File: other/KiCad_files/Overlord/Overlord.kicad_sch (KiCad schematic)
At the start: 108 parts, among them J1 RJ45x2, J2 Screw_Terminal_01x09, J3 Conn_01x12_Female, J4 Screw_Terminal_01x09, J5 Screw_Terminal_01x09, J6 Screw_Terminal_01x09, J7 USB_B, J8 USB_cable, Q1 2N7002E, Q2 2N7002E, Q3 2N7002E, Q4 2N7002E, U1 74HC4052D,653, U2 74HC4052D,653, U3 74HC4052D,653, U4 74HC4052D,653, U5 LM2575D2T-5G, U6 SN65HVD230, U7 MAX485ESA+T, U8 AP63203WU-7, U9 MAX485ESA+T

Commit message: temp changes
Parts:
- L2: footprint Inductor_SMD:L_Bourns-SRU8028_8.0x8.0mm -> (none)
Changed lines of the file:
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@@
       (effects (font (size 1.27 1.27)))
     )
-    (property "Footprint" "Inductor_SMD:L_Bourns-SRU8028_8.0x8.0mm" (at 60.96 247.65 0)
+    (property "Footprint" "" (at 60.96 247.65 0)
       (effects (font (size 1.27 1.27)) hide)
     )

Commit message: pre ESP32-S3 migration
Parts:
- U7, U9: value MAX485ESA+T -> MAX485ESA+T

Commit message: sent to production
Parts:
- removed 120R_enable1: Conn_01x02_Male, Connector_PinHeader_2.54mm:PinHeader_1x02_P2.54mm_Vertical, symbol Connector:Conn_01x02_Pin
- removed C1: 100uF, Capacitor_SMD:C_Elec_6.3x7.7, symbol Device:C_Polarized
- removed C17, C2, C3: 10uF, Capacitor_THT:CP_Radial_D4.0mm_P1.50mm, symbol Device:C_Polarized
- removed C18, C19, C20, C21, C22, C23, C24, C25, C26, C28, C29, C30, C31, C32, C33, C34, C35, C36, C37, C38, C39, C40, C41, C42, C43: 100nF, Capacitor_THT:C_Disc_D6.0mm_W2.5mm_P5.00mm, symbol Device:C
- removed C27, C44, C45: 220uF, Capacitor_THT:CP_Radial_D8.0mm_P3.50mm, symbol Device:C
- removed C5, C6: 22uF, Capacitor_THT:CP_Radial_D4.0mm_P1.50mm, symbol Device:C_Polarized
- removed D1: 1N5819, Diode_SMD:D_SOD-123, symbol Device:D_Schottky
- removed D2: SBR1A40S1, Diode_SMD:D_SOD-123, symbol Device:D
- removed ESP1: ESP-DevKitC-V4, Overlord:ESP32-DevKitC-V4, symbol MCU_Espressif_ESP32:ESP-DevKitC-V4
- removed J1: RJ45x2, Connector_RJ:RJ45_Amphenol_RJHSE538X-02, symbol Overlord-cache:74HC251D,653_RJ45x2
- removed J2, J5, J6: Screw_Terminal_01x09, TerminalBlockCustom:TerminalBlock_9_5.08mm_inverted, symbol Connector:Screw_Terminal_01x09
- removed J3: Conn_01x12_Female, Connector_Molex:Molex_CLIK-Mate_502386-1270_1x12-1MP_P1.25mm_Horizontal, symbol Connector_Generic_MountingPin:Conn_01x12_MountingPin
- removed J4: Screw_Terminal_01x09, TerminalBlockCustom:TerminalBlock_9_5.08mm, symbol Connector:Screw_Terminal_01x09
- removed J7: USB_B, Connector_USB:USB_B_OST_USB-B1HSxx_Horizontal, symbol Connector:USB_B
- removed J8: USB_cable, Connector_PinHeader_2.54mm:PinHeader_1x04_P2.54mm_Vertical, symbol Overlord-cache:Connector_Conn_01x04_Male
- removed L1: 7447709331, Inductor_SMD:L_12x12mm_H8mm, symbol Device:L
- removed L2: 4.7uH, symbol Device:L
- removed Q1, Q2, Q3, Q4: 2N7002E, Package_TO_SOT_SMD:SOT-23, symbol Transistor_FET:2N7002E
- removed R15: 10K, Resistor_SMD:R_0805_2012Metric_Pad1.20x1.40mm_HandSolder, symbol Device:R
- removed R16: 220, Resistor_SMD:R_0805_2012Metric_Pad1.20x1.40mm_HandSolder, symbol Device:R
- removed R31, R33: 5K, Resistor_SMD:R_0805_2012Metric_Pad1.20x1.40mm_HandSolder, symbol Device:R
- removed R6: 20K, Resistor_SMD:R_1812_4532Metric_Pad1.30x3.40mm_HandSolder, symbol Device:R
- removed R7: 120, Resistor_SMD:R_1812_4532Metric_Pad1.30x3.40mm_HandSolder, symbol Device:R
- removed RN1, RN2, RN3, RN4, RN5, RN6, RN7, RN8: Res_network 4.7kOhm, Resistor_SMD:R_Array_Convex_4x0612, symbol Device:R_Pack04
- removed U1, U2, U3, U4: 74HC4052D,653, Package_SO:SO-16_3.9x9.9mm_P1.27mm, symbol Overlord-cache:74HC251D,653_74HC4052D,653
- removed U5: LM2575D2T-5G, Package_TO_SOT_SMD:TO-263-5_TabPin3, symbol Regulator_Switching:LM2575-5.0BU
- removed U6: SN65HVD230, Package_SO:SOIC-8_3.9x4.9mm_P1.27mm, symbol Interface_CAN_LIN:SN65HVD230
- removed U8: AP63203WU-7, Package_TO_SOT_SMD:TSOT-23-6, symbol Regulator_Switching:AP63203WU
- added 12VLED1, 3V3LED1, 5VLED1: LED, LED_SMD:LED_0805_2012Metric_Pad1.15x1.40mm_HandSolder, symbol Device:LED
- added BOOT1, RESET1: PTS810SJK250SMTR LFS, OverlordCommon:PTS810SJK250SMTRLFS, symbol Switch:SW_MEC_5E
- added C1, C17, C3: 0.1uF, Capacitor_SMD:C_0805_2012Metric_Pad1.18x1.45mm_HandSolder, symbol Device:C
- added C11, C2: 10uF, Capacitor_SMD:C_0805_2012Metric_Pad1.18x1.45mm_HandSolder, symbol Device:C
- added C5, C6: 1uF, Capacitor_SMD:C_0805_2012Metric_Pad1.18x1.45mm_HandSolder, symbol Device:C
- added D1, D2, D3, D4, D5, D6: 1N4148, Diode_SMD:D_0805_2012Metric_Pad1.15x1.40mm_HandSolder, symbol Diode:1N4148
- added D7: TPD2E001DZDR, OverlordCommon:TPD2E001DZDR, symbol TPD2E001DZDR:TPD2E001DZDR
- added DB9_IN1: 5788792-2, OverlordCommon:5788792, symbol 5788792-2:5788792-2
- added DB9_OUT1: 5747844-4, OverlordCommon:57478444, symbol 5747844-4:5747844-4
- added Dbg1, Dbg10, Dbg11, Dbg12, Dbg13, Dbg14, Dbg15, Dbg16, Dbg17, Dbg18, Dbg19, Dbg2, Dbg20, Dbg21, Dbg22, Dbg23, Dbg24, Dbg25, Dbg26, Dbg27, Dbg28, Dbg29, Dbg3, Dbg30, Dbg31, Dbg32, Dbg33, Dbg34, Dbg4, Dbg5, Dbg6, Dbg7, Dbg8, Dbg9: Connector_Conn_01x01_Male, Connector_PinHeader_2.54mm:PinHeader_1x01_P2.54mm_Vertical, symbol Overlord-cache:Connector_Conn_01x01_Male
- added J1, J2, J3: 39502-1011, OverlordCommon:SHDRRA11W80P0X350_1X11_3990X690X920P, symbol 39502-1011:39502-1011
- added J4: Conn_01x12_Pin, Connector_Molex:Molex_Picoflex_90325-0012_2x06_P1.27mm_Vertical, symbol Connector:Conn_01x12_Pin
- added J5: Conn_01x10_Pin, Connector_PinHeader_2.54mm:PinHeader_1x10_P2.54mm_Vertical, symbol Connector:Conn_01x10_Pin
- added J6, J7: Conn_01x11_Pin, Connector_PinHeader_2.54mm:PinHeader_1x11_P2.54mm_Vertical, symbol Connector:Conn_01x11_Pin
- added JP1, JP10, JP11, JP12, JP13, JP14, JP15, JP16, JP17, JP18, JP19, JP2, JP20, JP21, JP22, JP23, JP24, JP25, JP26, JP27, JP28, JP29, JP3, JP30, JP31, JP32, JP33, JP34, JP35, JP36, JP37, JP38, JP39, JP4, JP40, JP41, JP42, JP43, JP44, JP45, JP46, JP47, JP48, JP49, JP5, JP50, JP51, JP52, JP53, JP6, JP7, JP8, JP9: SolderJumper_2_Open, Jumper:SolderJumper-2_P1.3mm_Open_RoundedPad1.0x1.5mm, symbol Jumper:SolderJumper_2_Open
- added J_CAN120R1: Conn_01x02_Male, Connector_PinHeader_2.54mm:PinHeader_1x02_P2.54mm_Vertical, symbol Connector:Conn_01x02_Pin
- added J_JTAG1: FTSH-105-01-S-DV-K, OverlordCommon:FTSH-105-XX-YYY-DV-K, symbol FTSH-105-01-S-DV-K:FTSH-105-01-S-DV-K
- added J_JTAG3V3_1, J_PROG3V3_1: Conn_01x02_Pin, Connector_PinHeader_2.54mm:PinHeader_1x02_P2.54mm_Vertical, symbol Connector:Conn_01x02_Pin
- added J_PROG1: FTSH-103-01-S-DV-TR, OverlordCommon:FTSH-103-XX-YYY-DV-TR, symbol FTSH-103-01-S-DV-TR:FTSH-103-01-S-DV-TR
- added J_USB1: USB_B, OverlordCommon:USB, symbol Connector:USB_B
- added R11: 240, Resistor_SMD:R_0805_2012Metric, symbol Device:R
- added R12: 10k, Resistor_SMD:R_0805_2012Metric_Pad1.20x1.40mm_HandSolder, symbol Device:R
- added R13: 499, Resistor_SMD:R_0805_2012Metric_Pad1.20x1.40mm_HandSolder, symbol Device:R
- added R14: 147, Resistor_SMD:R_0805_2012Metric_Pad1.20x1.40mm_HandSolder, symbol Device:R
- added R19, R20: 220, Resistor_SMD:R_0805_2012Metric_Pad1.20x1.40mm_HandSolder, symbol Device:R
- added SN65HVD230_1: SN65HVD230, Package_SO:SOIC-8_3.9x4.9mm_P1.27mm, symbol Interface_CAN_LIN:SN65HVD230
- added SYM1, SYM2, SYM3: Terminal plug, OverlordCommon:39500-0011, symbol Graphic:Logo_Open_Hardware_Small
- added SYM4, SYM5: N6_logo_medium, OverlordCommon:Symbol_N6Industries_medium, symbol Graphic:Logo_Open_Hardware_Small
- added SYM6: WEEE, Symbol:WEEE-Logo_5.6x8mm_SilkScreen, symbol Graphic:Logo_Open_Hardware_Small
- added SYM7: CE, Symbol:CE-Logo_8.5x6mm_SilkScreen, symbol Graphic:Logo_Open_Hardware_Small
- added U_ESP32-S3-WROOM-1U-N16_1: ESP32S3-Wroom, PCM_Espressif:ESP32-S3-WROOM-1U, symbol ESP32S3-wroom:ESP32S3-Wroom
- added U_LM317_1, U_LM317_2: LM317_SOT-223, Package_TO_SOT_SMD:SOT-223-3_TabPin2, symbol Regulator_Linear:LM317_SOT-223
- added U_TRS3232EIPWR1: TRS3232EIPWR, OverlordCommon:SOP65P640X120-16N, symbol TRS3232EIPWR:TRS3232EIPWR
- C10: value 100nF -> 10uF; footprint Capacitor_THT:C_Disc_D6.0mm_W2.5mm_P5.00mm -> Capacitor_SMD:C_0805_2012Metric_Pad1.18x1.45mm_HandSolder
- C12, C14, C15, C16, C8, C9: value 100nF -> 0.1uF; footprint Capacitor_THT:C_Disc_D6.0mm_W2.5mm_P5.00mm -> Capacitor_SMD:C_0805_2012Metric_Pad1.18x1.45mm_HandSolder
- C13: value 220uF -> 0.1uF; footprint Capacitor_THT:CP_Radial_D8.0mm_P3.50mm -> Capacitor_SMD:C_0805_2012Metric_Pad1.18x1.45mm_HandSolder
- C4: value 100nF -> 1uF; footprint Capacitor_SMD:C_1812_4532Metric_Pad1.57x3.40mm_HandSolder -> Capacitor_SMD:C_0805_2012Metric_Pad1.18x1.45mm_HandSolder
- C7: value 100nF -> 1uF; footprint Capacitor_THT:C_Disc_D6.0mm_W2.5mm_P5.00mm -> Capacitor_SMD:C_0805_2012Metric_Pad1.18x1.45mm_HandSolder
- H1, H2: now left out of the parts list
- R1: value 5K -> 240; footprint Resistor_SMD:R_0805_2012Metric_Pad1.20x1.40mm_HandSolder -> Resistor_SMD:R_0805_2012Metric
- R10: renamed from R26; footprint Resistor_SMD:R_1812_4532Metric_Pad1.30x3.40mm_HandSolder -> Resistor_SMD:R_0805_2012Metric_Pad1.20x1.40mm_HandSolder
- R15: renamed from R25; footprint Resistor_SMD:R_1812_4532Metric_Pad1.30x3.40mm_HandSolder -> Resistor_SMD:R_0805_2012Metric_Pad1.20x1.40mm_HandSolder
- R16: renamed from R30; footprint Resistor_SMD:R_1812_4532Metric_Pad1.30x3.40mm_HandSolder -> Resistor_SMD:R_0805_2012Metric_Pad1.20x1.40mm_HandSolder
- R17: value 220 -> 680; footprint Resistor_SMD:R_0805_2012Metric_Pad1.20x1.40mm_HandSolder -> Resistor_SMD:R_0805_2012Metric
- R2: value 5K -> 120
- R21: renamed from R13; footprint Resistor_SMD:R_1812_4532Metric_Pad1.30x3.40mm_HandSolder -> Resistor_SMD:R_0805_2012Metric_Pad1.20x1.40mm_HandSolder
- R22: renamed from R8; footprint Resistor_SMD:R_1812_4532Metric_Pad1.30x3.40mm_HandSolder -> Resistor_SMD:R_0805_2012Metric_Pad1.20x1.40mm_HandSolder
- R23: renamed from R11; footprint Resistor_SMD:R_1812_4532Metric_Pad1.30x3.40mm_HandSolder -> Resistor_SMD:R_0805_2012Metric_Pad1.20x1.40mm_HandSolder
- R24: renamed from R12; footprint Resistor_SMD:R_1812_4532Metric_Pad1.30x3.40mm_HandSolder -> Resistor_SMD:R_0805_2012Metric_Pad1.20x1.40mm_HandSolder
- R25: renamed from R10; footprint Resistor_SMD:R_1812_4532Metric_Pad1.30x3.40mm_HandSolder -> Resistor_SMD:R_0805_2012Metric_Pad1.20x1.40mm_HandSolder
- R26: renamed from R9; footprint Resistor_SMD:R_1812_4532Metric_Pad1.30x3.40mm_HandSolder -> Resistor_SMD:R_0805_2012Metric_Pad1.20x1.40mm_HandSolder
- R27: renamed from R14; footprint Resistor_SMD:R_1812_4532Metric_Pad1.30x3.40mm_HandSolder -> Resistor_SMD:R_0805_2012Metric_Pad1.20x1.40mm_HandSolder
- R3: value 10K -> 0R
- R4: value 10K -> 60
- R5: value 10K -> 390; footprint Resistor_SMD:R_0805_2012Metric_Pad1.20x1.40mm_HandSolder -> Resistor_SMD:R_0805_2012Metric
- R6: renamed from R29; footprint Resistor_SMD:R_1812_4532Metric_Pad1.30x3.40mm_HandSolder -> Resistor_SMD:R_0805_2012Metric_Pad1.20x1.40mm_HandSolder
- R7: renamed from R24; footprint Resistor_SMD:R_1812_4532Metric_Pad1.30x3.40mm_HandSolder -> Resistor_SMD:R_0805_2012Metric_Pad1.20x1.40mm_HandSolder
- R8: renamed from R27; footprint Resistor_SMD:R_1812_4532Metric_Pad1.30x3.40mm_HandSolder -> Resistor_SMD:R_0805_2012Metric_Pad1.20x1.40mm_HandSolder
- R9: renamed from R28; footprint Resistor_SMD:R_1812_4532Metric_Pad1.30x3.40mm_HandSolder -> Resistor_SMD:R_0805_2012Metric_Pad1.20x1.40mm_HandSolder
- renumbered U9 to MAX485ESA+T_1, U7 to MAX485ESA+T_2
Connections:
- net +12V: now also 12VLED1.2 (A), D2.2 (A), D6.2 (A), DB9_IN1.9, DB9_OUT1.9, Dbg33.1 (Pin_1); no longer R1.2, R2.2
- net +3.3V: now also C13.1, R1.1, 3V3LED1.2 (A), C1.1, C2.2, C3.1, C5.1, D1.2 (A), Dbg27.1 (Pin_1), J_JTAG3V3_1.2 (Pin_2), J_PROG3V3_1.1 (Pin_1), R12.2, SN65HVD230_1.3 (VCC), U_ESP32-S3-WROOM-1U-N16_1.2 (3.3), U_LM317_1.2 (VO), U_TRS3232EIPWR1.16 (VCC); no longer C12.2, C13.2
- net +5V: now also C10.1, C7.1, 5VLED1.2 (A), C11.1, D4.1 (K), D5.2 (A), Dbg30.1 (Pin_1), R11.1, U_LM317_2.2 (VO)
- net 1_1Y0: now also J3.11, J7.1 (Pin_1); no longer C14.2
- net 1_1Y1: now also J3.8, J7.4 (Pin_4); no longer C7.2
- net 1_1Y2: now also J3.10, J7.2 (Pin_2); no longer C8.1
- net 1_1Y3: now also J3.9, J7.3 (Pin_3); no longer C15.1
- net 1_2Y0: now also J3.6, J7.6 (Pin_6)
- net 1_2Y1: now also J3.5, J7.7 (Pin_7)
- net 1_2Y2: now also J3.4, J7.8 (Pin_8)
- net 1_2Y3: now also J3.7, J7.5 (Pin_5)
- net 2_1Y0: now also J3.3, J7.9 (Pin_9); no longer C16.2
- net 2_1Y1: now also J2.11, J6.1 (Pin_1); no longer C9.2
- net 2_1Y2: now also J3.2, J7.10 (Pin_10); no longer C10.1
- net 2_1Y3: now also J3.1, J7.11 (Pin_11)
- net 2_2Y0: now also J2.9, J6.3 (Pin_3)
- net 2_2Y1: now also J2.8, J6.4 (Pin_4)
- net 2_2Y2: now also J2.7, J6.5 (Pin_5)
- net 2_2Y3: now also J2.10, J6.2 (Pin_2)
- net 3_1Y0: now also J2.6, J6.6 (Pin_6)
- net 3_1Y1: now also J2.3, J6.9 (Pin_9)
- net 3_1Y2: now also J2.5, J6.7 (Pin_7)
- net 3_1Y3: now also J2.4, J6.8 (Pin_8)
- net 3_2Y0: now also J2.1, J6.11 (Pin_11)
- net 3_2Y1: now also J1.11, J5.1 (Pin_1)
- net 3_2Y2: now also J1.10, J5.2 (Pin_2)
- net 3_2Y3: now also J2.2, J6.10 (Pin_10)
- net 4_1Y0: now also J1.9, J5.3 (Pin_3)
- net 4_1Y1: now also J1.6, J5.6 (Pin_6)
- net 4_1Y2: now also J1.8, J5.4 (Pin_4)
- net 4_1Y3: now also J1.7, J5.5 (Pin_5)
- net 4_2Y0: now also J1.4, J5.8 (Pin_8)
- net 4_2Y1: now also J1.3, J5.9 (Pin_9)
- net 4_2Y2: now also J1.2, J5.10 (Pin_10)
- net 4_2Y3: now also J1.5, J5.7 (Pin_7)
- net CAN_H: now also R2.1, DB9_IN1.7, DB9_OUT1.7, Dbg22.1 (Pin_1), J4.8 (Pin_8), SN65HVD230_1.7 (CANH)
- net CAN_L: now also DB9_IN1.2, DB9_OUT1.2, Dbg24.1 (Pin_1), J4.9 (Pin_9), J_CAN120R1.1 (Pin_1), SN65HVD230_1.6 (CANL)
- net CAN_RX: now also Dbg21.1 (Pin_1), JP4.2 (B), SN65HVD230_1.4 (R); no longer R5.2
- net CAN_TX: now also Dbg20.1 (Pin_1), JP6.2 (B), SN65HVD230_1.1 (D); no longer R3.2
- net GND: now also C12.2, C13.2, C15.1, C4.2, C7.2, C9.2, R17.2, R3.1, R4.2, R5.2, BOOT1.2, C1.2, C11.2, C17.1, C2.1, C3.2, C5.2, C6.2, D7.1 (GND), DB9_IN1.1, DB9_IN1.10, DB9_IN1.11, DB9_OUT1.1, DB9_OUT1.10, DB9_OUT1.11, Dbg19.1 (Pin_1), J1.1, J4.7 (Pin_7), JP40.1 (A), JP42.1 (A), JP44.1 (A), JP46.1 (A), JP51.2 (B), J_USB1.4 (GND), J_USB1.5 (Shield), R13.2, R14.2, RESET1.2, SN65HVD230_1.2 (GND), U_ESP32-S3-WROOM-1U-N16_1.1 (GND), U_ESP32-S3-WROOM-1U-N16_1.40 (GND), U_ESP32-S3-WROOM-1U-N16_1.41 (GND), U_TRS3232EIPWR1.10 (DIN2), U_TRS3232EIPWR1.15 (GND), U_TRS3232EIPWR1.7 (DOUT2), U_TRS3232EIPWR1.8 (RIN2), U_TRS3232EIPWR1.9 (ROUT2); no longer C12.1, C13.1, C14.1, C15.2, C16.1, C7.1, C9.1
- net MB_DIR_CTRL_U1: now also Dbg4.1 (Pin_1), JP30.2 (B)
- net MB_DIR_CTRL_U2: now also Dbg14.1 (Pin_1), JP31.2 (B)
- net MB_RX_U1: now also Dbg2.1 (Pin_1), JP16.2 (B)
- net MB_RX_U2: now also Dbg12.1 (Pin_1), JP28.2 (B)
- net MB_TX_U1: now also Dbg6.1 (Pin_1), JP18.2 (B)
- net MB_TX_U2: now also Dbg16.1 (Pin_1), JP29.2 (B)
- net S0: now also JP26.2 (B)
- net S1: now also JP27.2 (B)
- net STATUS_LED_B: now also Dbg31.1 (Pin_1), JP34.2 (B), R20.2; no longer R18.2
- net STATUS_LED_G: now also Dbg29.1 (Pin_1), JP33.2 (B), R19.2; no longer R17.2
- net STATUS_LED_R: now also R18.2, Dbg28.1 (Pin_1), JP32.2 (B)
- net UART_RX_0: now also JP52.1 (A), JP7.2 (B), U_TRS3232EIPWR1.13 (RIN1)
- net UART_TX_0: now also JP5.2 (B), JP50.1 (A), U_TRS3232EIPWR1.11 (DIN1)
- net Y1: now also Dbg1.1 (Pin_1), JP17.2 (B)
- net Y2: now also Dbg3.1 (Pin_1), JP19.2 (B)
- net Y3: now also Dbg5.1 (Pin_1), JP14.2 (B)
- net Y4: now also Dbg7.1 (Pin_1), JP12.2 (B)
- net Y5: now also Dbg9.1 (Pin_1), JP8.2 (B)
- net Y6: now also Dbg11.1 (Pin_1), JP10.2 (B)
- net Y7: now also Dbg13.1 (Pin_1), JP21.2 (B)
- net Y8: now also Dbg15.1 (Pin_1), JP23.2 (B)
- net at C4.1: now also D1.1 (K), D2.1 (K), D3.1 (K), U_LM317_1.3 (VI)
- net at R5.1: now also R1.2, U_LM317_1.1 (ADJ)
- net at R4.1: now also 3V3LED1.1 (K)
- net at R17.1: now also R11.2, U_LM317_2.1 (ADJ)
- net at R18.1: now also J4.12 (Pin_12)
- net MB_A_1+ renamed MB1_H
- net MB1_H: now also DB9_IN1.8, DB9_OUT1.8, Dbg8.1 (Pin_1), J4.3 (Pin_3)
- net MB_A_2+ renamed MB2_H
- net MB2_H: now also DB9_IN1.5, DB9_OUT1.5, Dbg17.1 (Pin_1), J4.1 (Pin_1)
- net MB_B_1- renamed MB1_L
- net MB1_L: now also DB9_IN1.6, DB9_OUT1.6, Dbg10.1 (Pin_1), J4.4 (Pin_4)
- net MB_B_2- renamed MB2_L
- net MB2_L: now also DB9_IN1.4, DB9_OUT1.4, Dbg18.1 (Pin_1), J4.2 (Pin_2); no longer R4.2
- new net: JP45.1 (A), J_JTAG1.8
- new net: JP6.1 (A), U_ESP32-S3-WROOM-1U-N16_1.5 (IO5)
- new net: JP39.1 (A), J_JTAG1.2
- new net: JP18.1 (A), U_ESP32-S3-WROOM-1U-N16_1.11 (IO18)
- new net: JP37.1 (A), U_ESP32-S3-WROOM-1U-N16_1.26 (IO45)
- new net: JP40.2 (B), J_JTAG1.3
- new net: JP16.1 (A), U_ESP32-S3-WROOM-1U-N16_1.10 (IO17)
- new net: JP20.1 (A), U_ESP32-S3-WROOM-1U-N16_1.12 (IO8)
- new net: JP22.1 (A), U_ESP32-S3-WROOM-1U-N16_1.13 (IO19)
- new net: JP24.1 (A), U_ESP32-S3-WROOM-1U-N16_1.14 (IO20)
- new net: JP26.1 (A), U_ESP32-S3-WROOM-1U-N16_1.15 (IO3)
- new net: JP27.1 (A), U_ESP32-S3-WROOM-1U-N16_1.16 (IO46)
- new net: JP28.1 (A), U_ESP32-S3-WROOM-1U-N16_1.17 (IO9)
- new net: JP29.1 (A), U_ESP32-S3-WROOM-1U-N16_1.18 (IO10)
- new net: JP30.1 (A), U_ESP32-S3-WROOM-1U-N16_1.19 (IO11)
- new net: JP31.1 (A), U_ESP32-S3-WROOM-1U-N16_1.20 (IO12)
- new net: JP32.1 (A), U_ESP32-S3-WROOM-1U-N16_1.21 (IO13)
- new net: JP33.1 (A), U_ESP32-S3-WROOM-1U-N16_1.22 (IO14)
- new net: JP34.1 (A), U_ESP32-S3-WROOM-1U-N16_1.23 (IO21)
- new net: JP35.1 (A), U_ESP32-S3-WROOM-1U-N16_1.24 (IO47)
- new net: JP36.1 (A), U_ESP32-S3-WROOM-1U-N16_1.25 (IO48)
- new net: JP25.1 (A), U_ESP32-S3-WROOM-1U-N16_1.27 (IO0)
- new net: JP23.1 (A), U_ESP32-S3-WROOM-1U-N16_1.28 (IO35)
- new net: JP21.1 (A), U_ESP32-S3-WROOM-1U-N16_1.29 (IO36)
- new net: JP2.1 (A), U_ESP32-S3-WROOM-1U-N16_1.3 (EN)
- new net: JP19.1 (A), U_ESP32-S3-WROOM-1U-N16_1.30 (IO37)
- new net: JP17.1 (A), U_ESP32-S3-WROOM-1U-N16_1.31 (IO38)
- new net: JP15.1 (A), U_ESP32-S3-WROOM-1U-N16_1.32 (IO39)
- new net: JP13.1 (A), U_ESP32-S3-WROOM-1U-N16_1.33 (IO40)
- new net: JP11.1 (A), U_ESP32-S3-WROOM-1U-N16_1.34 (IO41)
- new net: JP9.1 (A), U_ESP32-S3-WROOM-1U-N16_1.35 (IO42)
- new net: JP7.1 (A), U_ESP32-S3-WROOM-1U-N16_1.36 (RXD0)
- new net: JP5.1 (A), U_ESP32-S3-WROOM-1U-N16_1.37 (TXD0)
- new net: JP3.1 (A), U_ESP32-S3-WROOM-1U-N16_1.38 (IO2)
- new net: JP1.1 (A), U_ESP32-S3-WROOM-1U-N16_1.39 (IO1)
- new net: JP4.1 (A), U_ESP32-S3-WROOM-1U-N16_1.4 (IO4)
- new net: JP8.1 (A), U_ESP32-S3-WROOM-1U-N16_1.6 (IO6)
- new net: JP10.1 (A), U_ESP32-S3-WROOM-1U-N16_1.7 (IO7)
- new net: JP12.1 (A), U_ESP32-S3-WROOM-1U-N16_1.8 (IO15)
- new net: JP14.1 (A), U_ESP32-S3-WROOM-1U-N16_1.9 (IO16)
- new net: C6.1, D5.1 (K), D6.1 (K), U_LM317_2.3 (VI)
- new net: JP44.2 (B), J_JTAG1.7
- new net: JP41.1 (A), J_JTAG1.4
- new net: JP53.1 (A), J_PROG1.6
- new net: 12VLED1.1 (K), R13.1
- new net: JP50.2 (B), J_PROG1.3
- new net: JP38.1 (A), J_JTAG3V3_1.1 (Pin_1)
- new net: JP38.2 (B), J_JTAG1.1
- new net: JP49.2 (B), J_PROG3V3_1.2 (Pin_2)
- new net: JP42.2 (B), J_JTAG1.5
- new net: C15.2, U_TRS3232EIPWR1.2 (V+)
- new net: J4.10 (Pin_10), R20.1
- new net: J4.11 (Pin_11), R19.1
- new net: J_CAN120R1.2 (Pin_2), R2.2
- new net: R3.2, SN65HVD230_1.8 (Rs)
- new net: C17.2, U_TRS3232EIPWR1.6 (V-)
- new net: JP51.1 (A), J_PROG1.4
- new net: JP47.1 (A), J_JTAG1.10
- new net: JP43.1 (A), J_JTAG1.6
- new net: 5VLED1.1 (K), R14.1
- new net: C14.1, U_TRS3232EIPWR1.1 (C1+)
- new net: C14.2, U_TRS3232EIPWR1.3 (C1-)
- new net: C16.2, U_TRS3232EIPWR1.4 (C2+)
- new net: C16.1, U_TRS3232EIPWR1.5 (C2-)
- new net: JP46.2 (B), J_JTAG1.9
- new net: JP48.2 (B), J_PROG1.1
- new net: JP49.1 (A), J_PROG1.2
- new net: JP52.2 (B), J_PROG1.5
- new net D+: D7.2 (IO1), JP24.2 (B), J_USB1.3 (D+)
- new net D-: D7.3 (IO2), JP22.2 (B), J_USB1.2 (D-)
- new net ESP_EN: C8.1, Dbg25.1 (Pin_1), JP2.2 (B), JP48.1 (A), R12.1, RESET1.4 (A)
- new net ESP_IO0: BOOT1.4 (A), C9.1, Dbg26.1 (Pin_1), JP25.2 (B), JP53.2 (B)
- new net JTAG_TCK: JP15.2 (B), JP41.2 (B)
- new net JTAG_TDI: JP11.2 (B), JP45.2 (B)
- new net JTAG_TDO: JP13.2 (B), JP43.2 (B)
- new net JTAG_TMS: JP39.2 (B), JP9.2 (B)
- new net Pin3: DB9_IN1.3, DB9_OUT1.3
- new net RS232_RX: Dbg32.1 (Pin_1), J4.6 (Pin_6), U_TRS3232EIPWR1.12 (ROUT1)
- new net RS232_TX: Dbg34.1 (Pin_1), J4.5 (Pin_5), U_TRS3232EIPWR1.14 (DOUT1)
- new net USB+5V: C12.1, D3.2 (A), D4.2 (A), D7.4 (VCC), Dbg23.1 (Pin_1), J_USB1.1 (VBUS)
- no-connect marks 13 -> 12
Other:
- added sheet InputMux (InputMux.kicad_sch)
- added sheet InputMux1 (InputMux.kicad_sch)
- added sheet InputMux2 (InputMux.kicad_sch)
- added sheet InputMux3 (InputMux.kicad_sch)
- note added: "Debug points"
- note added: "Microcontroller"
- note added: "Power and communication connection"
- note added: "Power conversion 3V3"
- note added: "Power conversion 5V"
- note added: "User connection interface"
- note removed: "1 – white/orange - CAN H 2 – orange - CAN L 3 – white/green - NC 4 – blue – CAN V+ 5 – white/blue – CAN GND 6 – green - NC 7 – white/brown – CAN GND 8 – brown – CAN V+"
- note removed: "1 – white/orange - MODBUS 2 A+ 2 – orange - MODBUS 2 B- 3 – white/green - MODBUS 0 A+ 4 – blue – +5V 5 – white/blue – GND 6 – green - MODBUS 0 B- 7 – white/brown – GND 8 – brown – +3.3V"
- note removed: "3V3 voltage regulator"
- note removed: "5V voltage regulator"
- note removed: "Connection interface"
- note removed: "ESP32-DevKitC Module"
- note removed: "RJ45 MODBUS connection"
- note removed: "RJ45 power and CAN communication connection"
- note removed: "USB connection"
- moved on the sheet: MAX485ESA+T_1, MAX485ESA+T_2, R10, R15, R16, R21, R22, R23, R24, R25, R26, R27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

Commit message: sent to production with fixes
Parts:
- removed 3V3LED1: LED, LED_SMD:LED_0805_2012Metric_Pad1.15x1.40mm_HandSolder, symbol Device:LED
- removed C5: 1uF, Capacitor_SMD:C_0805_2012Metric_Pad1.18x1.45mm_HandSolder, symbol Device:C
- removed D3, D6: 1N4148, Diode_SMD:D_0805_2012Metric_Pad1.15x1.40mm_HandSolder, symbol Diode:1N4148
- removed H1, H2: MountingHole, MountingHole:MountingHole_3.5mm, symbol Mechanical:MountingHole
- removed JP39, JP40, JP41, JP42, JP43, JP44, JP45, JP46, JP47, JP48, JP50, JP51, JP52, JP53: SolderJumper_2_Open, Jumper:SolderJumper-2_P1.3mm_Open_RoundedPad1.0x1.5mm, symbol Jumper:SolderJumper_2_Open
- removed J_JTAG3V3_1, J_PROG3V3_1: Conn_01x02_Pin, Connector_PinHeader_2.54mm:PinHeader_1x02_P2.54mm_Vertical, symbol Connector:Conn_01x02_Pin
- removed R1: 240, Resistor_SMD:R_0805_2012Metric, symbol Device:R
- removed R4: 60, Resistor_SMD:R_0805_2012Metric_Pad1.20x1.40mm_HandSolder, symbol Device:R
- removed R5: 390, Resistor_SMD:R_0805_2012Metric, symbol Device:R
- added 3V3LED2: LED, LED_SMD:LED_0805_2012Metric_Pad1.15x1.40mm_HandSolder, symbol Device:LED
- added C54, C55: 1uF, Capacitor_SMD:C_0805_2012Metric_Pad1.18x1.45mm_HandSolder, symbol Device:C
- added J8, J9: Conn_01x04_Pin, OverlordCommon:Solder_select_2x2, symbol Connector:Conn_01x04_Pin
- added R60: 240, Resistor_SMD:R_0805_2012Metric, symbol Device:R
- added R61: 60, Resistor_SMD:R_0805_2012Metric_Pad1.20x1.40mm_HandSolder, symbol Device:R
- added R62: 390, Resistor_SMD:R_0805_2012Metric, symbol Device:R
- added U_LM317_3: LM317_SOT-223, Package_TO_SOT_SMD:SOT-223-3_TabPin2, symbol Regulator_Linear:LM317_SOT-223
- D4: value 1N4148 -> SD0805S020S1R0
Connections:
- net +12V: now also C6.1, D2.1 (K), D5.1 (K), DB9_IN1.6, U_LM317_2.3 (VI), C54.1, U_LM317_3.3 (VI); no longer D2.2 (A), DB9_IN1.9
- net +3.3V: now also D2.2 (A), JP38.1 (A), JP49.2 (B), 3V3LED2.2 (A), C55.1, R60.1, U_LM317_3.2 (VO)
- net CAN_H: now also DB9_IN1.8; no longer DB9_IN1.7
- net CAN_L: now also DB9_IN1.4; no longer DB9_IN1.2
- net ESP_EN: now also J_PROG1.1
- net ESP_IO0: now also J_PROG1.6
- net GND: now also DB9_IN1.5, J_JTAG1.3, J_JTAG1.5, J_JTAG1.7, J_JTAG1.9, J_PROG1.4, C54.2, C55.2, R61.2, R62.2; no longer DB9_IN1.1
- net JTAG_TCK: now also J_JTAG1.4
- net JTAG_TDI: now also J_JTAG1.8
- net JTAG_TDO: now also J_JTAG1.6
- net JTAG_TMS: now also J_JTAG1.2
- net MB1_H: now also DB9_IN1.7; no longer DB9_IN1.8
- net MB1_L: now also DB9_IN1.9; no longer DB9_IN1.6
- net MB2_H: now also DB9_IN1.1; no longer DB9_IN1.5
- net MB2_L: now also DB9_IN1.2; no longer DB9_IN1.4
- net RS232_RX: now also J8.3 (Pin_3); no longer U_TRS3232EIPWR1.12 (ROUT1)
- net RS232_TX: now also J8.4 (Pin_4); no longer U_TRS3232EIPWR1.14 (DOUT1)
- net UART_RX_0: now also J_PROG1.5, J9.3 (Pin_3); no longer U_TRS3232EIPWR1.13 (RIN1)
- net UART_TX_0: now also J_PROG1.3, J9.4 (Pin_4); no longer U_TRS3232EIPWR1.11 (DIN1)
- net USB+5V: now also C4.1, D1.1 (K), U_LM317_1.3 (VI)
- net V_ADJ: now reaches U_LM317_1.1 (ADJ)
- net V_ADJ: now also R60.2, R62.1, U_LM317_3.1 (ADJ)
- new net: J9.1 (Pin_1), U_TRS3232EIPWR1.11 (DIN1)
- new net: J9.2 (Pin_2), U_TRS3232EIPWR1.12 (ROUT1)
- new net: 3V3LED2.1 (K), R61.1
- new net: J8.1 (Pin_1), U_TRS3232EIPWR1.13 (RIN1)
- new net: J8.2 (Pin_2), U_TRS3232EIPWR1.14 (DOUT1)
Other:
- note added: "Power conversion 12V -> 3V3"
- note added: "Power conversion 12V->5V"
- note added: "Power conversion 5V->3V3"
- note removed: "Power conversion 3V3"
- note removed: "Power conversion 5V"
- moved on the sheet: 12VLED1, 5VLED1, C13, C4, C6, C7, D1, D4, D5, R11, R13, R14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

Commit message: Sent for PCB production, ver 2.1 rev A
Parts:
- removed 12VLED1, 3V3LED2, 5VLED1: LED, LED_SMD:LED_0805_2012Metric_Pad1.15x1.40mm_HandSolder, symbol Device:LED
- removed C4, C54, C55, C6, C7: 1uF, Capacitor_SMD:C_0805_2012Metric_Pad1.18x1.45mm_HandSolder, symbol Device:C
- removed D1, D2, D5: 1N4148, Diode_SMD:D_0805_2012Metric_Pad1.15x1.40mm_HandSolder, symbol Diode:1N4148
- removed D4: SD0805S020S1R0, Diode_SMD:D_0805_2012Metric_Pad1.15x1.40mm_HandSolder, symbol Diode:1N4148
- removed J8, J9: Conn_01x04_Pin, OverlordCommon:Solder_select_2x2, symbol Connector:Conn_01x04_Pin
- removed J_USB1: USB_B, OverlordCommon:USB, symbol Connector:USB_B
- removed R11, R60: 240, Resistor_SMD:R_0805_2012Metric, symbol Device:R
- removed R13: 499, Resistor_SMD:R_0805_2012Metric_Pad1.20x1.40mm_HandSolder, symbol Device:R
- removed R14: 147, Resistor_SMD:R_0805_2012Metric_Pad1.20x1.40mm_HandSolder, symbol Device:R
- removed R17: 680, Resistor_SMD:R_0805_2012Metric, symbol Device:R
- removed R61: 60, Resistor_SMD:R_0805_2012Metric_Pad1.20x1.40mm_HandSolder, symbol Device:R
- removed R62: 390, Resistor_SMD:R_0805_2012Metric, symbol Device:R
- removed SYM7: CE, Symbol:CE-Logo_8.5x6mm_SilkScreen, symbol Graphic:Logo_Open_Hardware_Small
- removed U_LM317_1, U_LM317_2, U_LM317_3: LM317_SOT-223, Package_TO_SOT_SMD:SOT-223-3_TabPin2, symbol Regulator_Linear:LM317_SOT-223
- added J10: USB_B_Micro, Connector_USB:USB_Micro-B_Wuerth_614105150721_Vertical_CircularHoles, symbol Connector:USB_B_Micro
- added R1, R4: 499, Resistor_SMD:R_0805_2012Metric_Pad1.20x1.40mm_HandSolder, symbol Device:R
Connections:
- net D+: now also J10.3 (D+)
- net D-: now also J10.2 (D-)
- net GND: now also J10.5 (GND), J10.6 (Shield)
- net MB1_H: now also R4.2
- net MB1_L: now also R4.1
- net MB2_H: now also J4.2 (Pin_2), R1.2; no longer J4.1 (Pin_1)
- net MB2_L: now also J4.1 (Pin_1), R1.1; no longer J4.2 (Pin_2)
- net RS232_RX: now also U_TRS3232EIPWR1.14 (DOUT1)
- net RS232_TX: now also U_TRS3232EIPWR1.13 (RIN1)
- net UART_RX_0: now also U_TRS3232EIPWR1.12 (ROUT1)
- net UART_TX_0: now also U_TRS3232EIPWR1.11 (DIN1)
- net USB+5V: now also J10.1 (VBUS)
- no-connect marks 12 -> 13
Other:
- added sheet Power Conversion (PowerConversion.kicad_sch)
- note removed: "Power conversion 12V -> 3V3"
- note removed: "Power conversion 12V->5V"
- note removed: "Power conversion 5V->3V3"

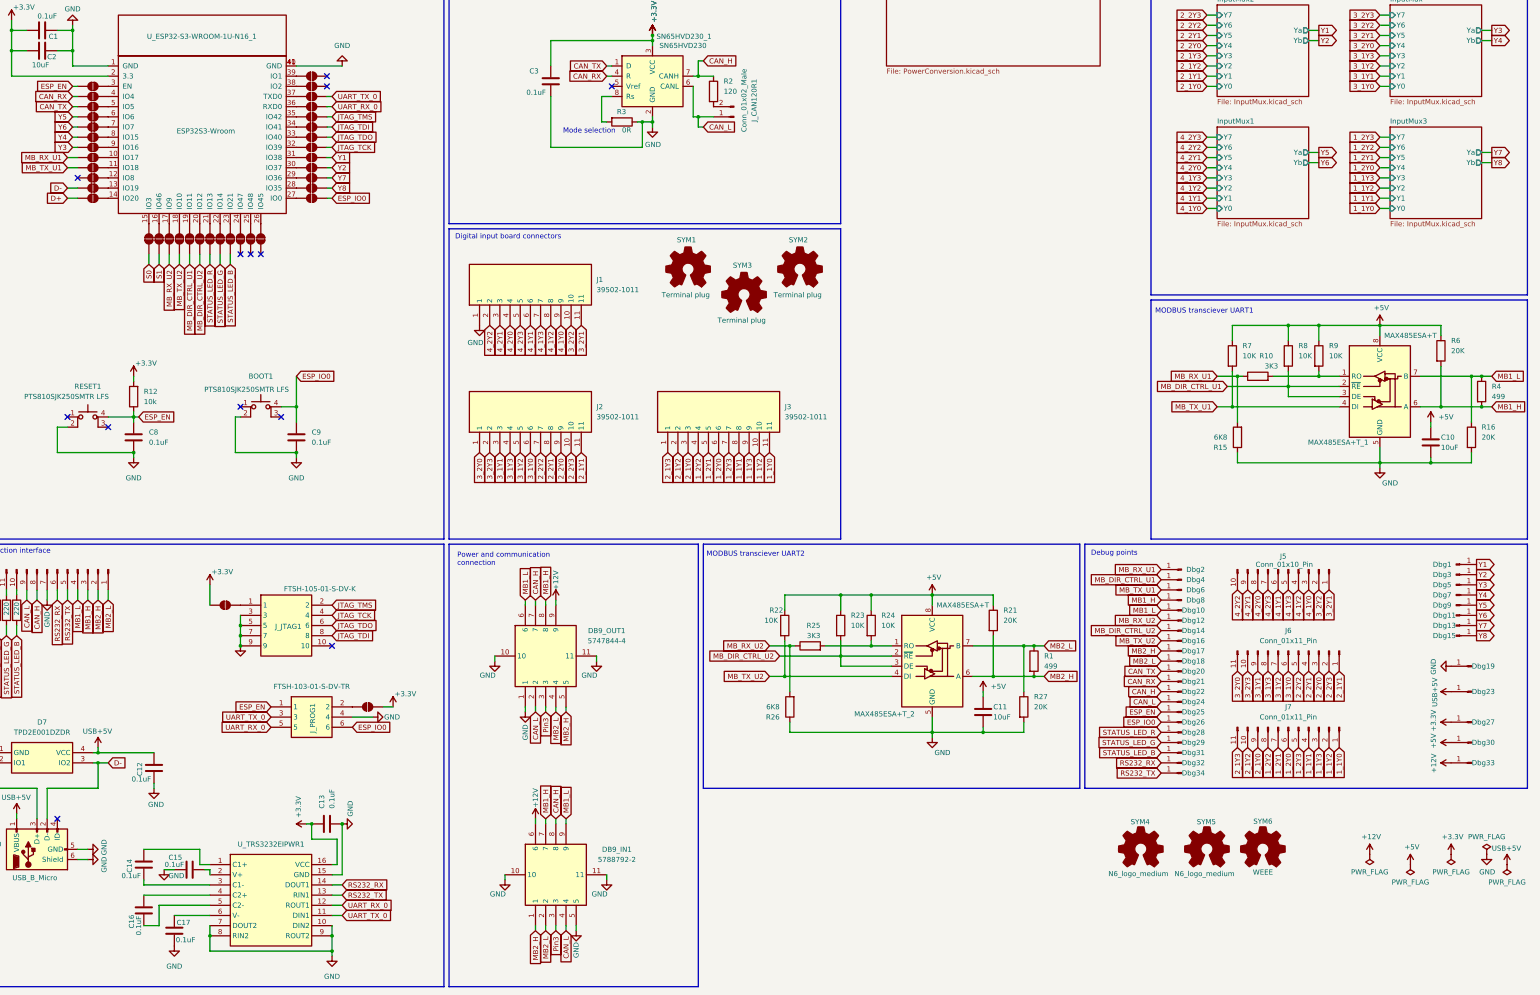
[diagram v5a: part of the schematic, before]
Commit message: Fixed PCB - changed modbus H/L to A/B - changed RS485 IC to a cheaper variant, fixed pullup resistors - added pullup on boot pin GPIO0 - removed unused power supplies and rerouted USB+5V for better voltage control - added transient voltage suppresion on digital inputs
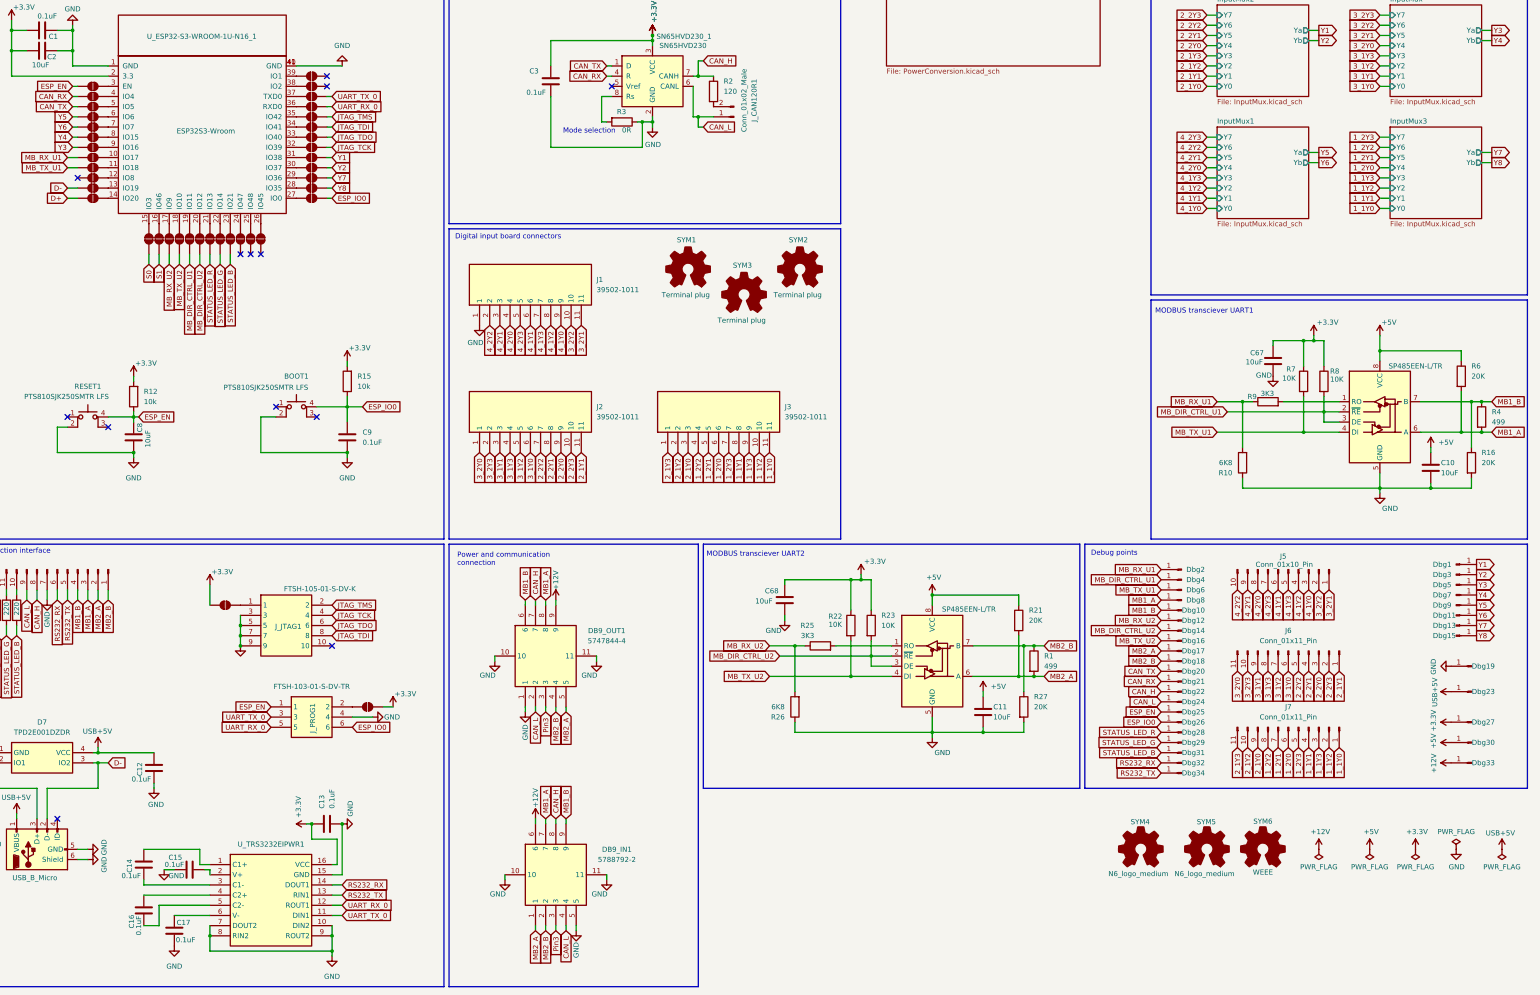
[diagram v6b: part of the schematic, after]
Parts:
- removed R24: 10K, Resistor_SMD:R_0805_2012Metric_Pad1.20x1.40mm_HandSolder, symbol Device:R
- added C67, C68: 10uF, Capacitor_SMD:C_0805_2012Metric_Pad1.18x1.45mm_HandSolder, symbol Device:C
- C8: value 0.1uF -> 10uF
- R10: value 3K3 -> 6K8
- R15: value 6K8 -> 10k
- R9: value 10K -> 3K3
- SP485EEN-L/TR_1: renamed from MAX485ESA+T_1; value MAX485ESA+T -> SP485EEN-L/TR
- SP485EEN-L/TR_2: renamed from MAX485ESA+T_2; value MAX485ESA+T -> SP485EEN-L/TR
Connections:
- net +3.3V: now also R15.2, R22.1, R23.1, R7.1, R8.1, C67.2, C68.2
- net +5V: no longer R22.1, R23.1, R7.1, R8.1, R9.1
- net ESP_IO0: now also R15.1
- net GND: now also R10.1, C67.1, C68.1; no longer R15.1
- net MB_RX_U1: now also R10.2, R9.1; no longer R10.1, R15.2
- net at R9.2, SP485EEN-L/TR_1.1 (RO): no longer R10.2
- net MB1_H renamed MB1_A
- net MB1_L renamed MB1_B
- net MB2_H renamed MB2_A
- net MB2_L renamed MB2_B
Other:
- moved on the sheet: BOOT1, C10, C9, R16, R21, R22, R23, R25, R26, R4, R6, R7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
